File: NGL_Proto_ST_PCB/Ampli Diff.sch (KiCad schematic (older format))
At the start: 30 parts, among them U7 AD620, U8 AD8639

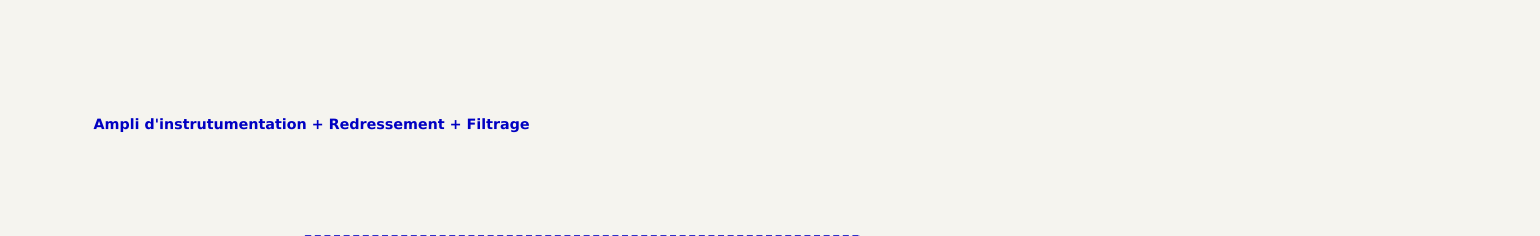
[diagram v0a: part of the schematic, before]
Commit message: Rrecherche sur pot num et mise en page
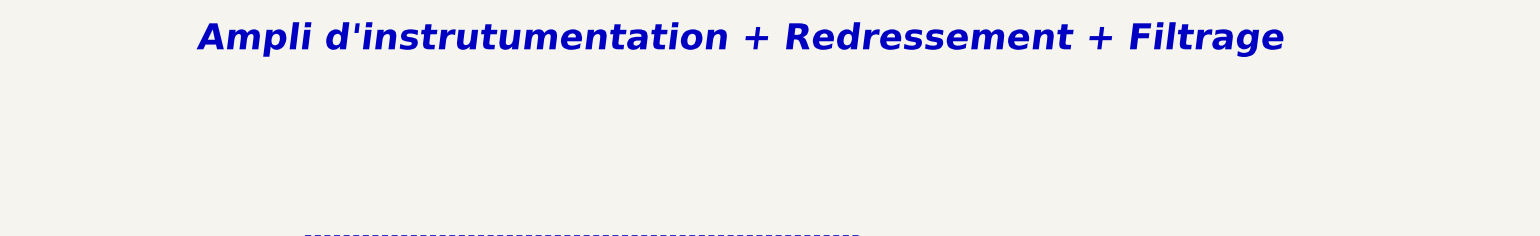
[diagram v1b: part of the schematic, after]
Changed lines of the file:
@@
 $Descr A4 11693 8268
 encoding utf-8
-Sheet 5 5
-Title ""
-Date ""
-Rev ""
-Comp ""
-Comment1 ""
-Comment2 ""
-Comment3 ""
+Sheet 6 6
+Title "NGL_Proto_V2"
+Date "2022-05-27"
+Rev "V2"
+Comp "ADTP"
+Comment1 "Auteur: Benoît"
+Comment2 "Proto avec potar numérique + intégration"
+Comment3 "Sous traité chez JLCPCB"
 Comment4 ""
 $EndDescr
@@
 Wire Wire Line
 	825  3850 825  3895
-Text Notes 1500 2000 0    79   ~ 16
+Text Notes 2280 1410 0    197  Italic 39
 Ampli d'instrutumentation + Redressement + Filtrage
 Wire Wire Line

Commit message: Commit avant DSN
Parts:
- C20, C21, C22, C23, C24, C25, C26, C27, C29: footprint Capacitor_SMD:C_0805_2012Metric -> Capacitor_SMD:C_0805_2012Metric_Pad1.18x1.45mm_HandSolder
- R16, R26, R27, R28, R29, R30, R31, R32, R33, R37: footprint Resistor_SMD:R_0805_2012Metric -> Resistor_SMD:R_0805_2012Metric_Pad1.20x1.40mm_HandSolder
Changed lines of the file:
@@
 encoding utf-8
 Sheet 6 6
-Title "NGL_Proto_V2"
-Date "2022-05-27"
-Rev "V2"
+Title "NGL_Proto_ST"
+Date "2022-06-09"
+Rev "V1.1"
 Comp "ADTP"
 Comment1 "Auteur: Benoît"
@@
 F 0 "R32" H 7790 4191 50  0000 L CNN
 F 1 "10K" H 7790 4100 50  0000 L CNN
-F 2 "Resistor_SMD:R_0805_2012Metric" V 7650 4145 50  0001 C CNN
+F 2 "Resistor_SMD:R_0805_2012Metric_Pad1.20x1.40mm_HandSolder" V 7650 4145 50  0001 C CNN
 F 3 "~" H 7720 4145 50  0001 C CNN
 	1    7720 4145
@@
 F 0 "R33" H 8255 4191 50  0000 L CNN
 F 1 "10K" H 8255 4100 50  0000 L CNN
-F 2 "Resistor_SMD:R_0805_2012Metric" V 8115 4145 50  0001 C CNN
+F 2 "Resistor_SMD:R_0805_2012Metric_Pad1.20x1.40mm_HandSolder" V 8115 4145 50  0001 C CNN
 F 3 "~" H 8185 4145 50  0001 C CNN
 	1    8185 4145
@@
 F 0 "C20" H 8070 4481 50  0000 L CNN
 F 1 "47uF" H 8070 4390 50  0000 L CNN
-F 2 "Capacitor_SMD:C_0805_2012Metric" H 7993 4285 50  0001 C CNN
+F 2 "Capacitor_SMD:C_0805_2012Metric_Pad1.18x1.45mm_HandSolder" H 7993 4285 50  0001 C CNN
 F 3 "~" H 7955 4435 50  0001 C CNN
 	1    7955 4435
@@
 F 0 "C21" H 8690 4481 50  0000 L CNN
 F 1 "47uF" H 8690 4390 50  0000 L CNN
-F 2 "Capacitor_SMD:C_0805_2012Metric" H 8613 4285 50  0001 C CNN
+F 2 "Capacitor_SMD:C_0805_2012Metric_Pad1.18x1.45mm_HandSolder" H 8613 4285 50  0001 C CNN
 F 3 "~" H 8575 4435 50  0001 C CNN
 	1    8575 4435
@@
 F 0 "R31" H 6790 3096 50  0000 L CNN
 F 1 "40K" H 6790 3005 50  0000 L CNN
-F 2 "Resistor_SMD:R_0805_2012Metric" V 6650 3050 50  0001 C CNN
+F 2 "Resistor_SMD:R_0805_2012Metric_Pad1.20x1.40mm_HandSolder" V 6650 3050 50  0001 C CNN
 F 3 "~" H 6720 3050 50  0001 C CNN
 	1    6720 3050
@@
 F 0 "R28" H 4280 3096 50  0000 L CNN
 F 1 "40K" H 4280 3005 50  0000 L CNN
-F 2 "Resistor_SMD:R_0805_2012Metric" V 4140 3050 50  0001 C CNN
+F 2 "Resistor_SMD:R_0805_2012Metric_Pad1.20x1.40mm_HandSolder" V 4140 3050 50  0001 C CNN
 F 3 "~" H 4210 3050 50  0001 C CNN
 	1    4210 3050
@@
 F 0 "R29" H 6280 4091 50  0000 L CNN
 F 1 "20K" H 6280 4000 50  0000 L CNN
-F 2 "Resistor_SMD:R_0805_2012Metric" V 6140 4045 50  0001 C CNN
+F 2 "Resistor_SMD:R_0805_2012Metric_Pad1.20x1.40mm_HandSolder" V 6140 4045 50  0001 C CNN
 F 3 "~" H 6210 4045 50  0001 C CNN
 	1    6210 4045
@@
 F 0 "R30" H 6430 4636 50  0000 L CNN
 F 1 "10K" H 6430 4545 50  0000 L CNN
-F 2 "Resistor_SMD:R_0805_2012Metric" V 6290 4590 50  0001 C CNN
+F 2 "Resistor_SMD:R_0805_2012Metric_Pad1.20x1.40mm_HandSolder" V 6290 4590 50  0001 C CNN
 F 3 "~" H 6360 4590 50  0001 C CNN
 	1    6360 4590
@@
 F 0 "R26" H 3795 4641 50  0000 L CNN
 F 1 "10K" H 3795 4550 50  0000 L CNN
-F 2 "Resistor_SMD:R_0805_2012Metric" V 3655 4595 50  0001 C CNN
+F 2 "Resistor_SMD:R_0805_2012Metric_Pad1.20x1.40mm_HandSolder" V 3655 4595 50  0001 C CNN
 F 3 "~" H 3725 4595 50  0001 C CNN
 	1    3725 4595
@@
 F 0 "R16" H 3645 4091 50  0000 L CNN
 F 1 "20K" H 3645 4000 50  0000 L CNN
-F 2 "Resistor_SMD:R_0805_2012Metric" V 3505 4045 50  0001 C CNN
+F 2 "Resistor_SMD:R_0805_2012Metric_Pad1.20x1.40mm_HandSolder" V 3505 4045 50  0001 C CNN
 F 3 "~" H 3575 4045 50  0001 C CNN
 	1    3575 4045
@@
 F 0 "R27" H 4275 3501 50  0000 L CNN
 F 1 "20K" H 4275 3410 50  0000 L CNN
-F 2 "Resistor_SMD:R_0805_2012Metric" V 4135 3455 50  0001 C CNN
+F 2 "Resistor_SMD:R_0805_2012Metric_Pad1.20x1.40mm_HandSolder" V 4135 3455 50  0001 C CNN
 F 3 "~" H 4205 3455 50  0001 C CNN
 	1    4205 3455
@@
 F 0 "C23" H 1335 6716 50  0000 L CNN
 F 1 "100nF" H 1335 6625 50  0000 L CNN
-F 2 "Capacitor_SMD:C_0805_2012Metric" H 1258 6520 50  0001 C CNN
+F 2 "Capacitor_SMD:C_0805_2012Metric_Pad1.18x1.45mm_HandSolder" H 1258 6520 50  0001 C CNN
 F 3 "~" H 1220 6670 50  0001 C CNN
 	1    1220 6670
@@
 F 0 "C22" H 1335 6351 50  0000 L CNN
 F 1 "100nF" H 1335 6260 50  0000 L CNN
-F 2 "Capacitor_SMD:C_0805_2012Metric" H 1258 6155 50  0001 C CNN
+F 2 "Capacitor_SMD:C_0805_2012Metric_Pad1.18x1.45mm_HandSolder" H 1258 6155 50  0001 C CNN
 F 3 "~" H 1220 6305 50  0001 C CNN
 	1    1220 6305
@@
 F 0 "C29" H 9185 4486 50  0000 L CNN
 F 1 "47uF" H 9185 4395 50  0000 L CNN
-F 2 "Capacitor_SMD:C_0805_2012Metric" H 9108 4290 50  0001 C CNN
+F 2 "Capacitor_SMD:C_0805_2012Metric_Pad1.18x1.45mm_HandSolder" H 9108 4290 50  0001 C CNN
 F 3 "~" H 9070 4440 50  0001 C CNN
 	1    9070 4440
@@
 F 0 "R37" H 8925 4191 50  0000 L CNN
 F 1 "10K" H 8925 4100 50  0000 L CNN
-F 2 "Resistor_SMD:R_0805_2012Metric" V 8785 4145 50  0001 C CNN
+F 2 "Resistor_SMD:R_0805_2012Metric_Pad1.20x1.40mm_HandSolder" V 8785 4145 50  0001 C CNN
 F 3 "~" H 8855 4145 50  0001 C CNN
 	1    8855 4145
@@
 F 0 "C24" H 5140 5976 50  0000 L CNN
 F 1 "4.7uF" H 5140 5885 50  0000 L CNN
-F 2 "Capacitor_SMD:C_0805_2012Metric" H 5063 5780 50  0001 C CNN
+F 2 "Capacitor_SMD:C_0805_2012Metric_Pad1.18x1.45mm_HandSolder" H 5063 5780 50  0001 C CNN
 F 3 "~" H 5025 5930 50  0001 C CNN
 	1    5025 5930
@@
 F 0 "C26" H 5580 5976 50  0000 L CNN
 F 1 "100nF" H 5580 5885 50  0000 L CNN
-F 2 "Capacitor_SMD:C_0805_2012Metric" H 5503 5780 50  0001 C CNN
+F 2 "Capacitor_SMD:C_0805_2012Metric_Pad1.18x1.45mm_HandSolder" H 5503 5780 50  0001 C CNN
 F 3 "~" H 5465 5930 50  0001 C CNN
 	1    5465 5930
@@
 F 0 "C25" H 5140 6351 50  0000 L CNN
 F 1 "4.7uF" H 5140 6260 50  0000 L CNN
-F 2 "Capacitor_SMD:C_0805_2012Metric" H 5063 6155 50  0001 C CNN
+F 2 "Capacitor_SMD:C_0805_2012Metric_Pad1.18x1.45mm_HandSolder" H 5063 6155 50  0001 C CNN
 F 3 "~" H 5025 6305 50  0001 C CNN
 	1    5025 6305
@@
 F 0 "C27" H 5580 6351 50  0000 L CNN
 F 1 "100nF" H 5580 6260 50  0000 L CNN
-F 2 "Capacitor_SMD:C_0805_2012Metric" H 5503 6155 50  0001 C CNN
+F 2 "Capacitor_SMD:C_0805_2012Metric_Pad1.18x1.45mm_HandSolder" H 5503 6155 50  0001 C CNN
 F 3 "~" H 5465 6305 50  0001 C CNN
 	1    5465 6305
